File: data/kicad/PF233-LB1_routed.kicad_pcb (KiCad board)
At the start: 4 copper layers, 78 x 77.2 mm, 83 parts, among them U1 74AHCT1G125, U2 74AHCT1G125

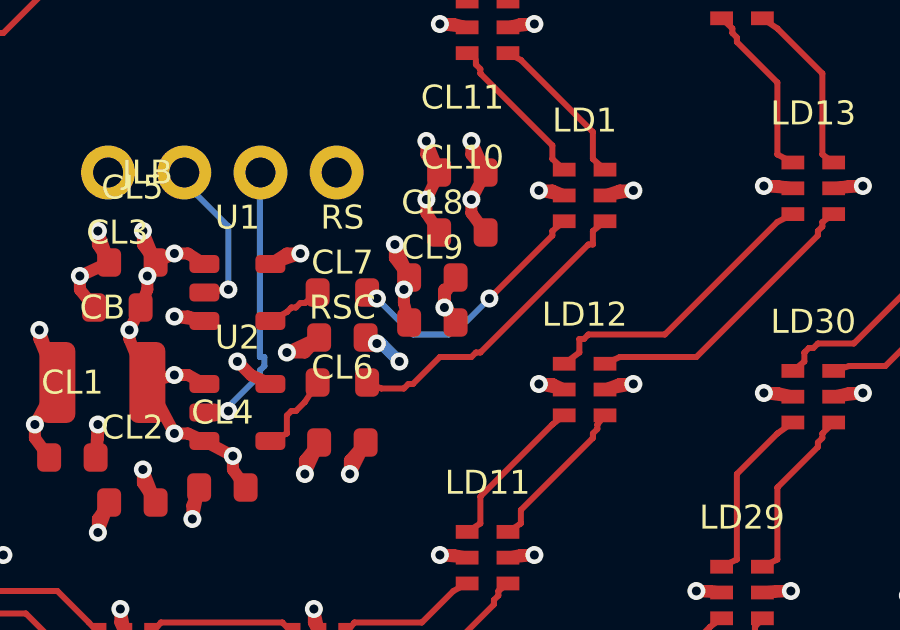
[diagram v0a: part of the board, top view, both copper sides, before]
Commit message: WIP: sign-off outputs (75 / 1 before the process-guard fix; deadline test and re-run in progress)
Co-Authored-By: Claude Opus 5.5 <noreply@anthropic.com>
Claude-Session: https://claude.ai/code/session_01FX4DWSYYjMCFGGA6gmha65
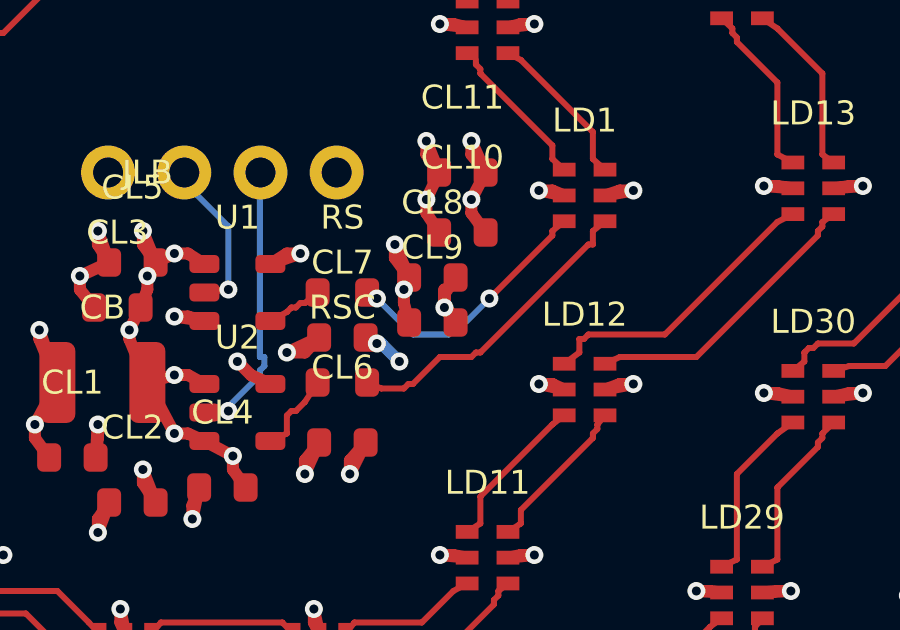
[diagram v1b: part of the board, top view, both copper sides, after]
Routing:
- net GND: track 154.1 -> 154.7 mm
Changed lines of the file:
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@@
   (segment (start 131.8500 114.1500) (end 132.0920 113.8710) (width 0.2) (layer "F.Cu") (net 67))
   (segment (start 107.4000 99.9000) (end 107.4000 100.5000) (width 0.4) (layer "F.Cu") (net 2))
+  (segment (start 107.4000 100.5000) (end 107.7750 101.0000) (width 0.4) (layer "F.Cu") (net 2))
   (via (at 110.5500 96.6000) (size 0.6) (drill 0.3) (layers "F.Cu" "B.Cu") (net 2))
   (via (at 107.2500 91.0500) (size 0.6) (drill 0.3) (layers "F.Cu" "B.Cu") (net 2))
